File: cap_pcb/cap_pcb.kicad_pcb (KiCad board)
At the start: 2 copper layers, 43 parts, among them U0 ATtiny85-20PU, U1 PCF8574, U10 HDSP-7803, U11 HDSP-7803, U12 PCF8574, U2 HDSP-7803, U3 PCF8574, U4 HDSP-7803, U5 PCF8574, U6 HDSP-7803, U7 PCF8574, U8 HDSP-7803, U9 PCF8574

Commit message: mostly finished pcb
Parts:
- moved R13 56.0 mm to (106.7, 32.9)
- moved R3 43.3 mm to (106.7, 76.3)
- moved R6 39.1 mm to (81.4, 87.4)
- moved R2 35.8 mm to (106.7, 42.9)
- moved C0 34.3 mm to (175.3, 92.5), turned to 270 degrees
- moved C8 34.3 mm to (148.6, 92.6), turned to 270 degrees
- moved C9 34.3 mm to (145.3, 92.6), turned to 270 degrees
- moved C1 34.3 mm to (179.3, 92.5), turned to 270 degrees
- moved C10 34.3 mm to (163.4, 92.5), turned to 270 degrees
- moved C13 34.2 mm to (159.5, 92.4), turned to 270 degrees
- moved C12 34.1 mm to (133.5, 92.4), turned to 270 degrees
- moved C4 33.8 mm to (206.1, 92.3), turned to 270 degrees
- moved C11 33.8 mm to (130.6, 92.3), turned to 270 degrees
- moved C3 33.7 mm to (194.1, 92.1), turned to 270 degrees
- moved C2 33.7 mm to (190.7, 92.1), turned to 270 degrees
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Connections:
- U5 pad 15: Net-(R1-Pad2) -> Net-(R0-Pad2)
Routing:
- net VCC: track 0.08 -> 346.8 mm
- net Net-(R12-Pad1): track 0.00 -> 171.3 mm
- net Net-(R10-Pad1): track 0.00 -> 156.5 mm
- net Net-(R3-Pad1): track 0.00 -> 144.7 mm
- net Net-(R8-Pad1): track 0.00 -> 126.3 mm
- net Net-(R1-Pad2): track 47.3 -> 167.1 mm
- net Net-(R13-Pad1): track 0.00 -> 111.7 mm
- net Net-(R6-Pad2): track 0.00 -> 111.6 mm
- net Net-(R4-Pad2): track 0.00 -> 99.5 mm
- net Net-(R11-Pad1): track 0.00 -> 98.0 mm
- net Net-(R2-Pad1): track 0.00 -> 84.7 mm
- net Net-(R9-Pad1): track 0.00 -> 68.3 mm
- net Net-(R0-Pad2): track 186.9 -> 249.1 mm
- net Net-(U11-Pad5): track 0.00 -> 58.9 mm
- net Net-(U5-Pad7): track 0.00 -> 56.7 mm
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- added copper zone on B.Cu, net GND
- added copper zone on F.Cu, net GND
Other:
- board outline added: 158 x 108.3 mm

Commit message: finalized pcb, added source folder
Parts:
- added R14: 10k, Resistor_THT:R_Axial_DIN0411_L9.9mm_D3.6mm_P25.40mm_Horizontal, F.Cu at (225.0, 119.4)
- added SW1: SW_MEC_5E, Button_Switch_THT:SW_MEC_5GTH9, F.Cu at (163.6, 106.7)
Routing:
- net Net-(R14-Pad1): track 0.00 -> 79.7 mm
- net Net-(SW1-Pad1): track 0.00 -> 59.9 mm
- removed copper zone on B.Cu, net GND
- removed copper zone on F.Cu, net GND

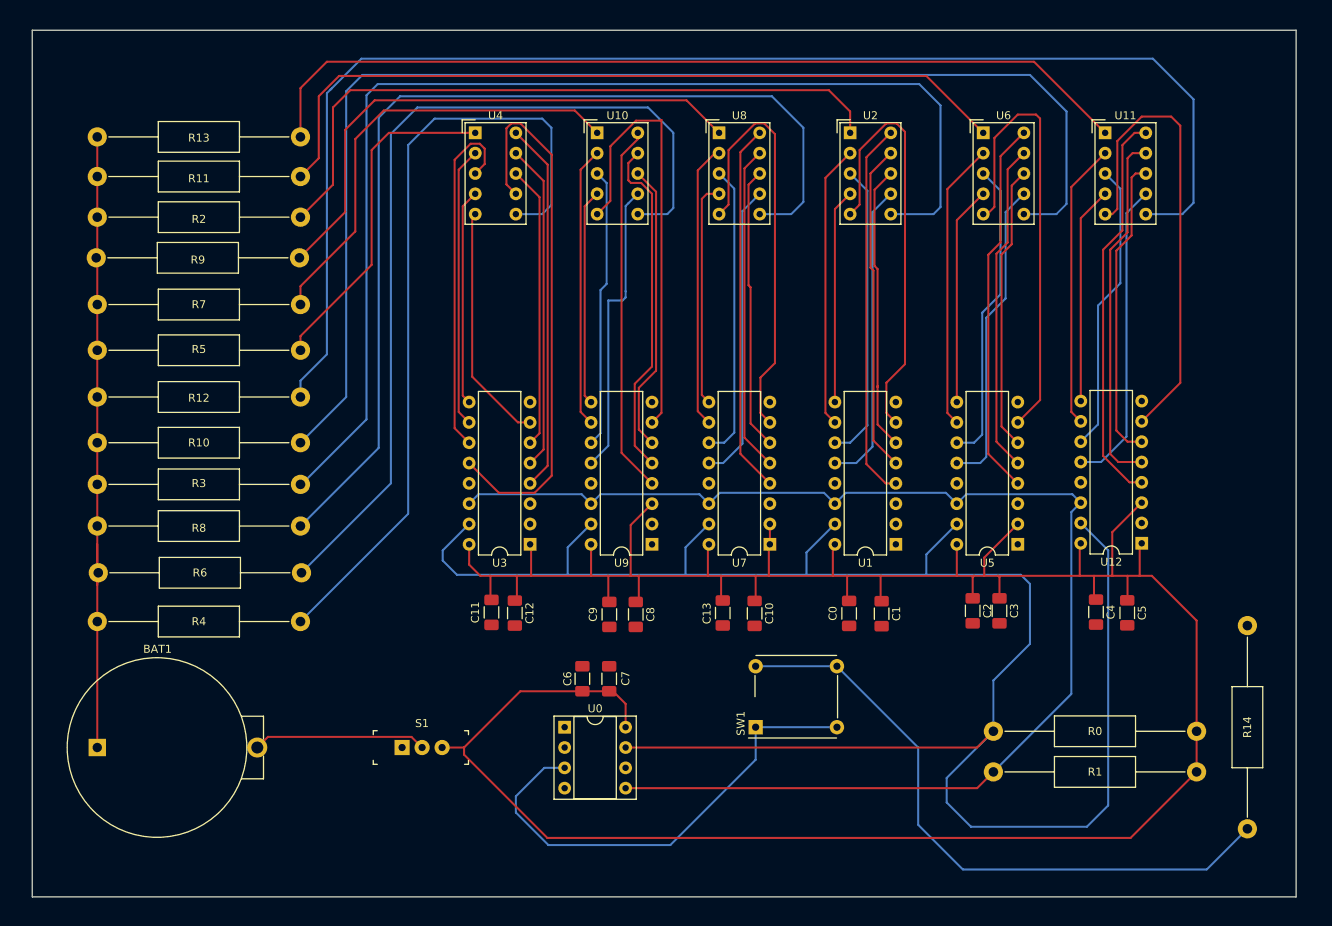
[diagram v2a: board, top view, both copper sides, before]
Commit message: fixed pcb to include proper ground (lol); added some src files for the attiny85
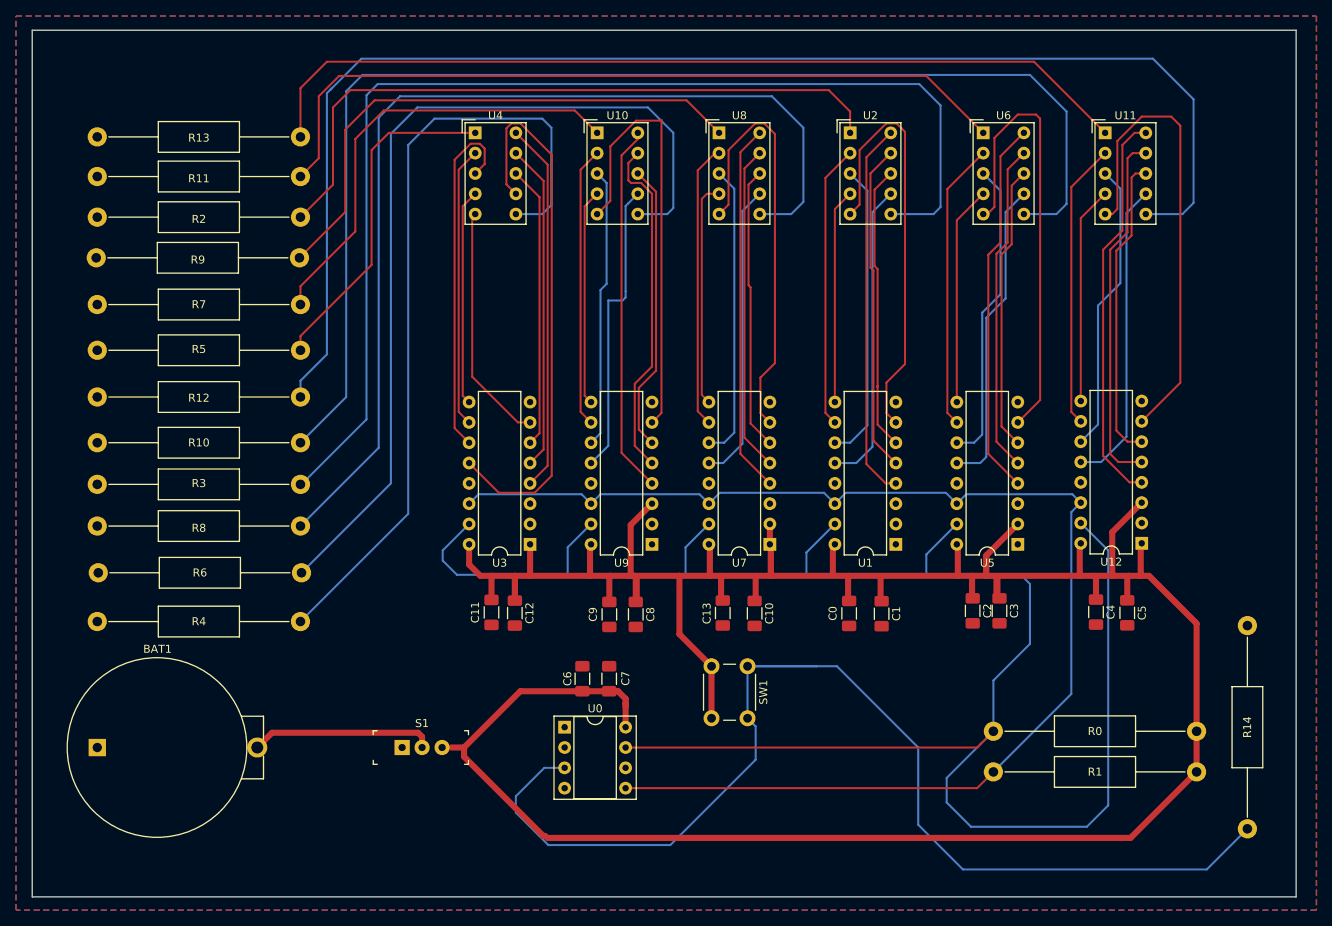
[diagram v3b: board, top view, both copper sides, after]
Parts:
- SW1: value SW_MEC_5E -> SW_Push; footprint Button_Switch_THT:SW_MEC_5GTH9 -> Button_Switch_THT:SW_PUSH_6mm
- moved SW1 7.69 mm to (162.6, 99.1), turned to 270 degrees
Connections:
- SW1 pad 1: Net-(SW1-Pad1) -> Net-(R14-Pad1)
- SW1 pad 2: Net-(R14-Pad1) -> VCC
- U0 pad 3: Net-(SW1-Pad1) -> Net-(R14-Pad1)
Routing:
- net VCC: track 346.8 -> 529.5 mm
- net GND: track 81.3 -> 0.00 mm
- net Net-(R14-Pad1): track 79.7 -> 146.2 mm
- net Net-(SW1-Pad1): track 59.9 -> 0.00 mm
- net Net-(BAT1-PadPos): track 21.7 -> 22.9 mm
- added copper zone on B.Cu, net GND
- added copper zone on F.Cu, net GND
